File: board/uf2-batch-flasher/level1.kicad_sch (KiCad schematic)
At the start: 6 parts, among them U102 FSUSB74, U103 74HC238

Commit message: Briefly document and add the OSHW logo.
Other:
- company: (none) -> nbp.name
- title: (none) -> UF2 Batch Flasher
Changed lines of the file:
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@@
 (kicad_sch (version 20230121) (generator eeschema)
   (paper "A4")
+  (title_block
+    (title "UF2 Batch Flasher")
+    (date "2023-10-20")
+    (rev "0.1")
+    (company "nbp.name")
+    (comment 2 "are dispatched to the leaves of the tree of USB devices.")
+    (comment 3 "This is the second level, where select flags and data lines")
+    (comment 4 "UF2 Batch Flasher is a USB hub for flashing USB devices")
+  )
   (junction (at 40.64 67.31) (diameter 0) (color 0 0 0 0)
   )

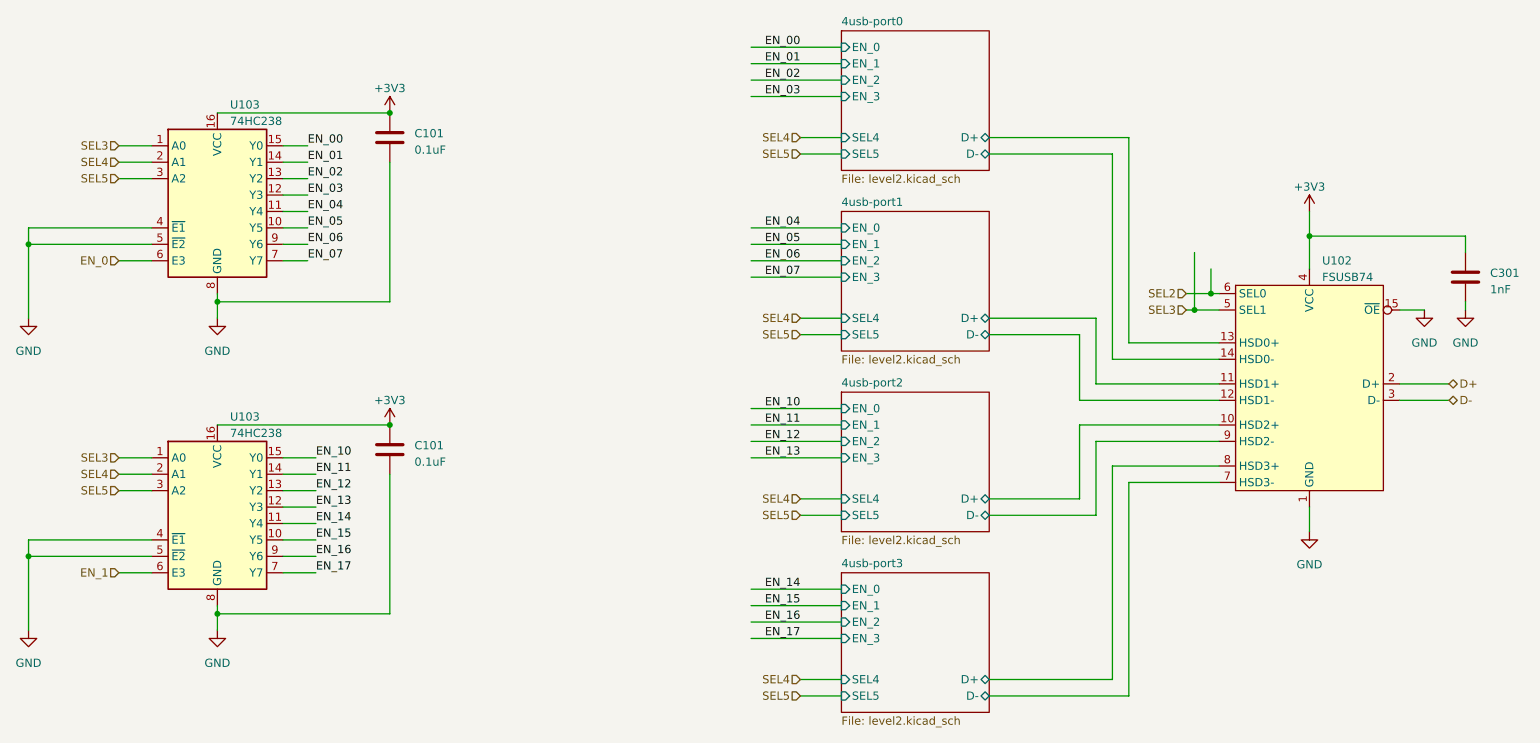
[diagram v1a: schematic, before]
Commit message: Fix Select pins mapping.
Both the selector and demultiplexer are used to enable/disable the power
and data pins. If the mapping of pins is not identical between the 2
then we would enable the power pins of one USB port and the data pins of
another.

This patch changes that such that components which are closer to the
Pico are using the high-power bits while components which are further
down the tree are using the low bits. This way the enable pins are
correctly ordered as specified in the datasheets of both components.

Previously we were using the lowest bits, this would have been if
the enable pins were mapped accordingly. Which was not the case.

This change include changes in the schematics and in the board layout.
The component remain at their original placement.

This change also adds the OSHW logo as well as the fiducial in the
schematic such that they are not removed each time we re-import the
schematics in the board.
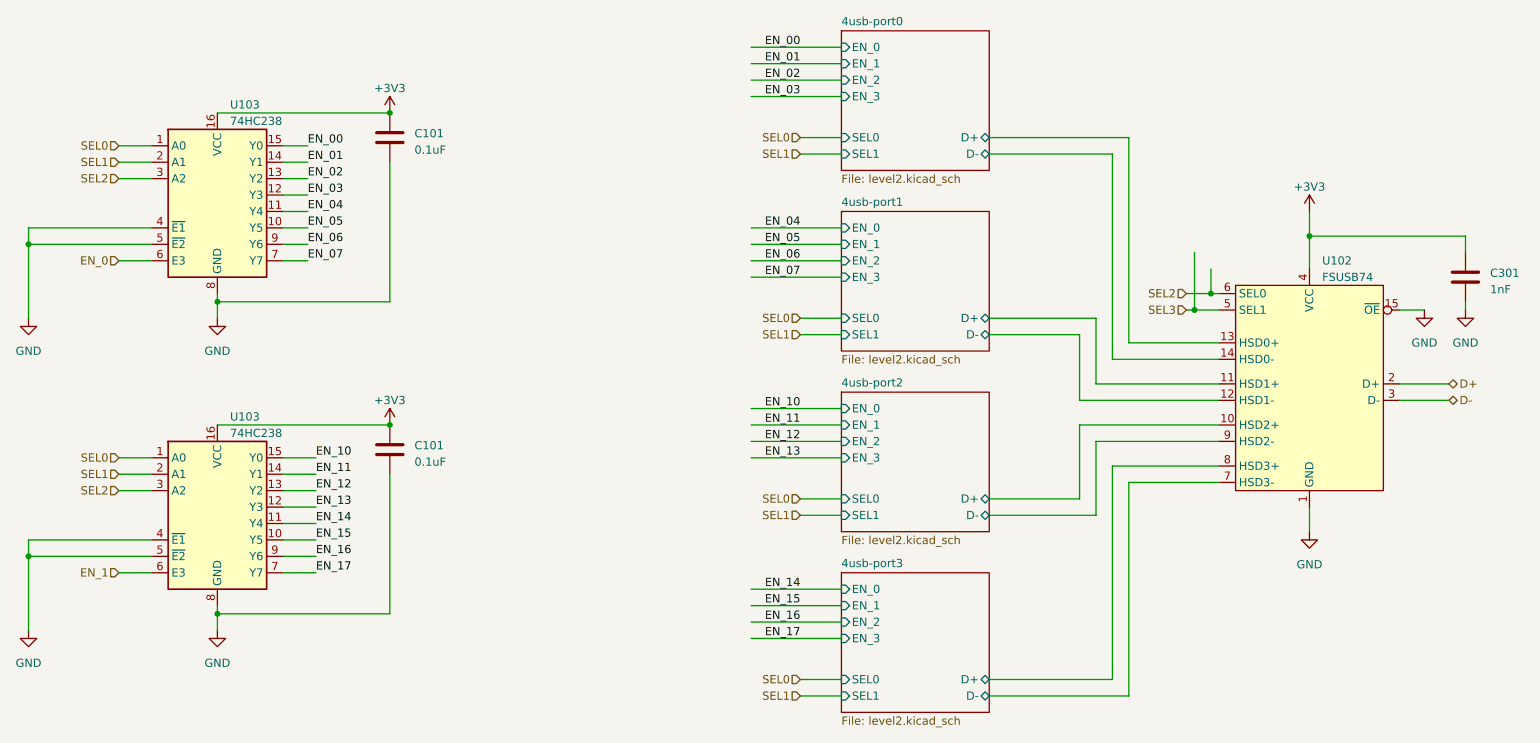
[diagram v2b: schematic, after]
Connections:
- net SEL5 is gone; now on net SEL2: U103.3 (A2), U103.3 (A2)
- net SEL3: no longer U103.1 (A0), U103.1 (A0)
- net SEL4 renamed SEL1
- new net SEL0: U103.1 (A0), U103.1 (A0)
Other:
- sheet 4usb-port0 ports: added SEL0, SEL1; removed SEL4, SEL5
- sheet 4usb-port1 ports: added SEL0, SEL1; removed SEL4, SEL5
- sheet 4usb-port2 ports: added SEL0, SEL1; removed SEL4, SEL5
- sheet 4usb-port3 ports: added SEL0, SEL1; removed SEL4, SEL5
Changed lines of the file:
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@@
     (effects (font (size 1.27 1.27)) (justify right bottom))
   )
-  (hierarchical_label "SEL4" (shape input) (at 160.02 50.8 180) (fields_autoplaced)
+  (hierarchical_label "SEL0" (shape input) (at 160.02 50.8 180) (fields_autoplaced)
     (effects (font (size 1.27 1.27)) (justify right))
   )
@@
     (effects (font (size 1.27 1.27)) (justify left))
   )
-  (hierarchical_label "SEL5" (shape input) (at 160.02 53.34 180) (fields_autoplaced)
-    (effects (font (size 1.27 1.27)) (justify right))
-  )
-  (hierarchical_label "SEL4" (shape input) (at 54.61 102.87 180) (fields_autoplaced)
-    (effects (font (size 1.27 1.27)) (justify right))
-  )
-  (hierarchical_label "SEL4" (shape input) (at 54.61 54.61 180) (fields_autoplaced)
-    (effects (font (size 1.27 1.27)) (justify right))
-  )
-  (hierarchical_label "SEL5" (shape input) (at 54.61 105.41 180) (fields_autoplaced)
+  (hierarchical_label "SEL1" (shape input) (at 160.02 53.34 180) (fields_autoplaced)
+    (effects (font (size 1.27 1.27)) (justify right))
+  )
+  (hierarchical_label "SEL2" (shape input) (at 54.61 105.41 180) (fields_autoplaced)
+    (effects (font (size 1.27 1.27)) (justify right))
+  )
+  (hierarchical_label "SEL0" (shape input) (at 54.61 100.33 180) (fields_autoplaced)
+    (effects (font (size 1.27 1.27)) (justify right))
+  )
+  (hierarchical_label "SEL1" (shape input) (at 54.61 54.61 180) (fields_autoplaced)
     (effects (font (size 1.27 1.27)) (justify right))
   )
@@
     (effects (font (size 1.27 1.27)) (justify left))
   )
-  (hierarchical_label "SEL4" (shape input) (at 160.02 134.62 180) (fields_autoplaced)
+  (hierarchical_label "SEL0" (shape input) (at 160.02 134.62 180) (fields_autoplaced)
     (effects (font (size 1.27 1.27)) (justify right))
   )
@@
     (effects (font (size 1.27 1.27)) (justify right))
   )
-  (hierarchical_label "SEL5" (shape input) (at 160.02 81.28 180) (fields_autoplaced)
+  (hierarchical_label "SEL1" (shape input) (at 160.02 81.28 180) (fields_autoplaced)
     (effects (font (size 1.27 1.27)) (justify right))
   )
@@
     (effects (font (size 1.27 1.27)) (justify right))
   )
-  (hierarchical_label "SEL5" (shape input) (at 160.02 137.16 180) (fields_autoplaced)
+  (hierarchical_label "SEL1" (shape input) (at 160.02 137.16 180) (fields_autoplaced)
     (effects (font (size 1.27 1.27)) (justify right))
   )
@@
     (effects (font (size 1.27 1.27)) (justify right))
   )
-  (hierarchical_label "SEL4" (shape input) (at 160.02 106.68 180) (fields_autoplaced)
-    (effects (font (size 1.27 1.27)) (justify right))
-  )
-  (hierarchical_label "SEL4" (shape input) (at 160.02 78.74 180) (fields_autoplaced)
-    (effects (font (size 1.27 1.27)) (justify right))
-  )
-  (hierarchical_label "SEL5" (shape input) (at 160.02 109.22 180) (fields_autoplaced)
+  (hierarchical_label "SEL1" (shape input) (at 54.61 102.87 180) (fields_autoplaced)
+    (effects (font (size 1.27 1.27)) (justify right))
+  )
+  (hierarchical_label "SEL0" (shape input) (at 160.02 106.68 180) (fields_autoplaced)
+    (effects (font (size 1.27 1.27)) (justify right))
+  )
+  (hierarchical_label "SEL0" (shape input) (at 160.02 78.74 180) (fields_autoplaced)
+    (effects (font (size 1.27 1.27)) (justify right))
+  )
+  (hierarchical_label "SEL1" (shape input) (at 160.02 109.22 180) (fields_autoplaced)
     (effects (font (size 1.27 1.27)) (justify right))
   )
@@
     (effects (font (size 1.27 1.27)) (justify right))
   )
-  (hierarchical_label "SEL3" (shape input) (at 54.61 52.07 180) (fields_autoplaced)
-    (effects (font (size 1.27 1.27)) (justify right))
-  )
-  (hierarchical_label "SEL5" (shape input) (at 54.61 57.15 180) (fields_autoplaced)
-    (effects (font (size 1.27 1.27)) (justify right))
-  )
-  (hierarchical_label "SEL3" (shape input) (at 54.61 100.33 180) (fields_autoplaced)
+  (hierarchical_label "SEL0" (shape input) (at 54.61 52.07 180) (fields_autoplaced)
+    (effects (font (size 1.27 1.27)) (justify right))
+  )
+  (hierarchical_label "SEL2" (shape input) (at 54.61 57.15 180) (fields_autoplaced)
     (effects (font (size 1.27 1.27)) (justify right))
   )
@@
       (effects (font (size 1.27 1.27)) (justify left))
     )
-    (pin "SEL4" input (at 166.37 134.62 180)
-      (effects (font (size 1.27 1.27)) (justify left))
-    )
-    (pin "SEL5" input (at 166.37 137.16 180)
+    (pin "SEL0" input (at 166.37 134.62 180)
+      (effects (font (size 1.27 1.27)) (justify left))
+    )
+    (pin "SEL1" input (at 166.37 137.16 180)
       (effects (font (size 1.27 1.27)) (justify left))
     )
@@
       (effects (font (size 1.27 1.27)) (justify left))
     )
-    (pin "SEL4" input (at 166.37 50.8 180)
-      (effects (font (size 1.27 1.27)) (justify left))
-    )
-    (pin "SEL5" input (at 166.37 53.34 180)
+    (pin "SEL0" input (at 166.37 50.8 180)
+      (effects (font (size 1.27 1.27)) (justify left))
+    )
+    (pin "SEL1" input (at 166.37 53.34 180)
       (effects (font (size 1.27 1.27)) (justify left))
     )
@@
       (effects (font (size 1.27 1.27)) (justify left))
     )
-    (pin "SEL4" input (at 166.37 106.68 180)
-      (effects (font (size 1.27 1.27)) (justify left))
-    )
-    (pin "SEL5" input (at 166.37 109.22 180)
+    (pin "SEL0" input (at 166.37 106.68 180)
+      (effects (font (size 1.27 1.27)) (justify left))
+    )
+    (pin "SEL1" input (at 166.37 109.22 180)
       (effects (font (size 1.27 1.27)) (justify left))
     )
@@
       (effects (font (size 1.27 1.27)) (justify left))
     )
-    (pin "SEL4" input (at 166.37 78.74 180)
-      (effects (font (size 1.27 1.27)) (justify left))
-    )
-    (pin "SEL5" input (at 166.37 81.28 180)
-      (effects (font (size 1.27 1.27)) (justify left))
-    )
+    (pin "SEL0" input (at 166.37 78.74 180)
+      (effects (font (size 1.27 1.27)) (justify left))
+    )
+    (pin "SEL1" input (at 166.37 81.28 180)
+      (effects (font (size 1.27 1.27)) (justify left))
+    )
